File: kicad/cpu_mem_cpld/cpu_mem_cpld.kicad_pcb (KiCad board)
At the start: 2 copper layers, 160 x 100.3 mm, 33 parts, among them CON1 BARREL_JACK, J1 USB, P5 CONN_02X25, SW1 SW_PUSH, U1 65C02, U2 XC95108PC84, U3 28C256, U4 AS6C4008-55PCN, U5 74HC245, U6 LM555N, U7 74HCT00, X1 OSC

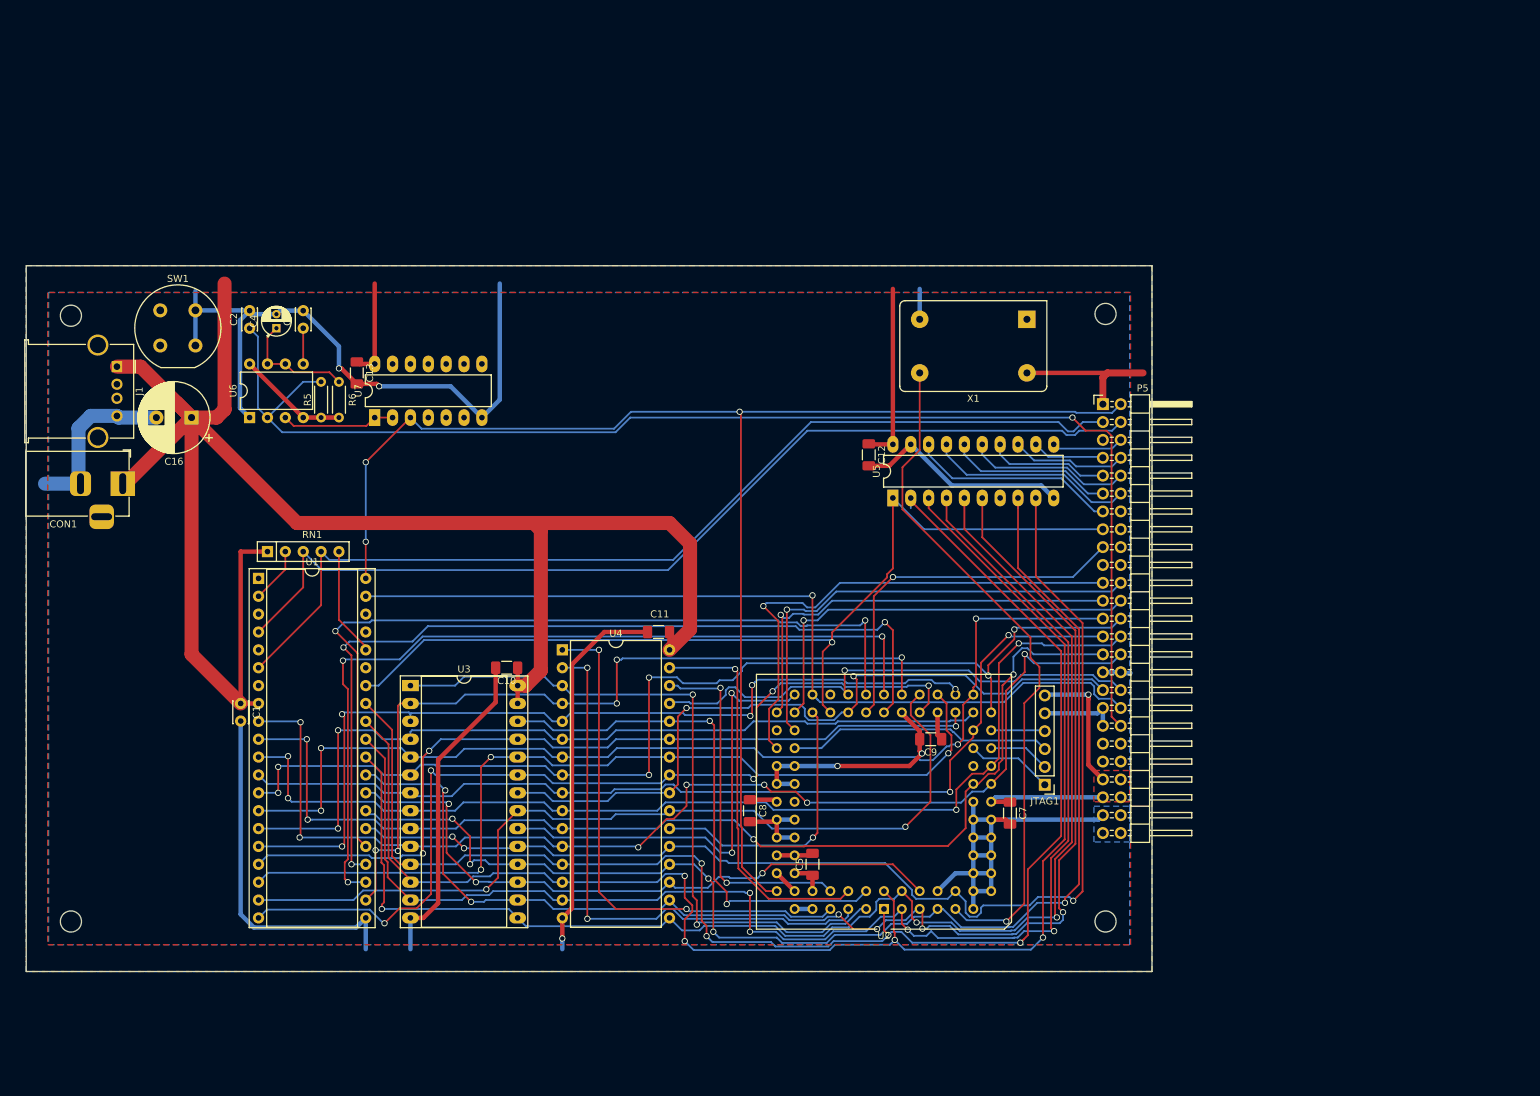
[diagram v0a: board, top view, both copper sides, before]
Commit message: cpld version with uart
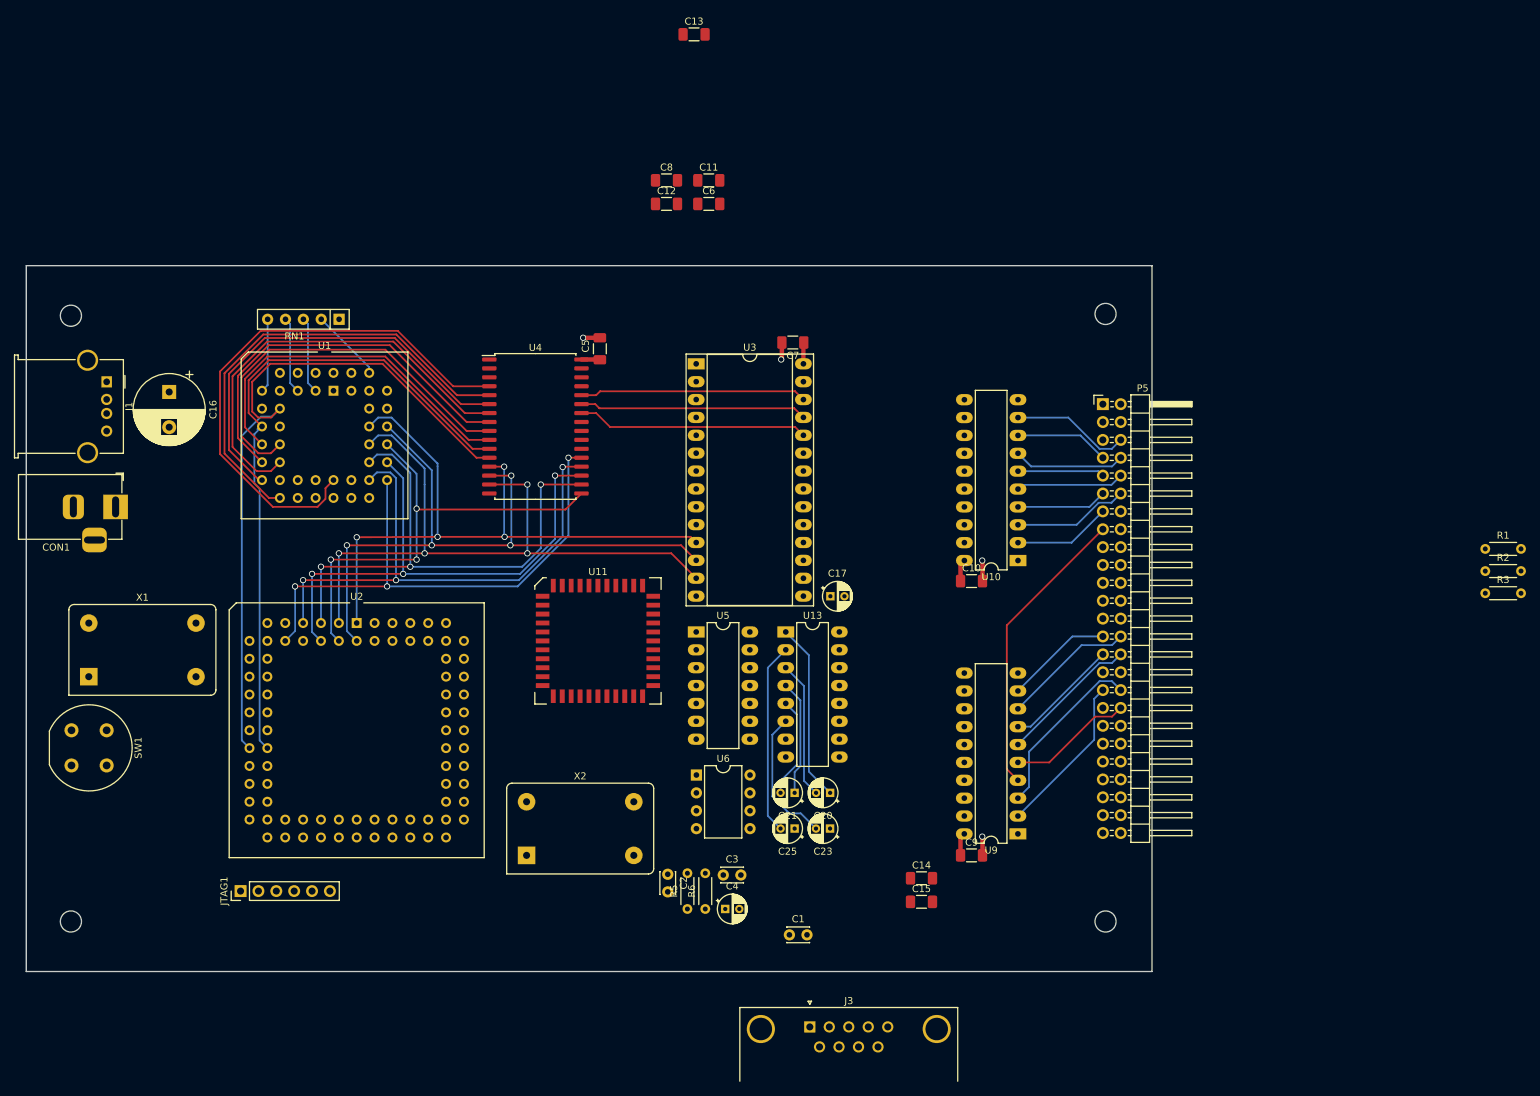
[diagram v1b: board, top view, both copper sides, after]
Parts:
- removed U7: 74HCT00, Package_DIP:DIP-14_W7.62mm_LongPads
- added C14: 100nF, Capacitor_SMD:C_1206_3216Metric_Pad1.33x1.80mm_HandSolder, F.Cu at (189.5, 132.8)
- added C15: 100nF, Capacitor_SMD:C_1206_3216Metric_Pad1.33x1.80mm_HandSolder, F.Cu at (189.5, 136.1)
- added C17: 1µF, Capacitor_THT:CP_Radial_D4.0mm_P2.00mm, F.Cu at (176.5, 92.7)
- added C20: 1µF, Capacitor_THT:CP_Radial_D4.0mm_P2.00mm, F.Cu at (176.5, 120.7)
- added C21: 1µF, Capacitor_THT:CP_Radial_D4.0mm_P2.00mm, F.Cu at (171.4, 120.7)
- added C23: 1µF, Capacitor_THT:CP_Radial_D4.0mm_P2.00mm, F.Cu at (176.5, 125.7)
- added C25: 1µF, Capacitor_THT:CP_Radial_D4.0mm_P2.00mm, F.Cu at (171.4, 125.7)
- added C6: 100n, Capacitor_SMD:C_1206_3216Metric_Pad1.33x1.80mm_HandSolder, F.Cu at (159.2, 36.9)
- added J3: DB9, Connector_Dsub:DSUB-9_Male_Horizontal_P2.77x2.84mm_EdgePinOffset4.94mm_Housed_MountingHolesOffset7.48mm, F.Cu at (173.6, 153.9)
- added R1: 4k7, Resistor_THT:R_Axial_DIN0204_L3.6mm_D1.6mm_P5.08mm_Horizontal, F.Cu at (269.6, 86.0)
- added R2: 4k7, Resistor_THT:R_Axial_DIN0204_L3.6mm_D1.6mm_P5.08mm_Horizontal, F.Cu at (269.6, 89.1)
- added R3: 3k3, Resistor_THT:R_Axial_DIN0204_L3.6mm_D1.6mm_P5.08mm_Horizontal, F.Cu at (269.6, 92.3)
- added U10: 74HC245, Package_DIP:DIP-20_W7.62mm_LongPads, F.Cu at (203.2, 87.6)
- added U11: 16550, Package_LCC:PLCC-44, F.Cu at (143.5, 99.1)
- added U13: MAX232, Package_DIP:DIP-16_W7.62mm_LongPads, F.Cu at (170.2, 97.8)
- added U9: 74HC245, Package_DIP:DIP-20_W7.62mm_LongPads, F.Cu at (203.2, 126.5)
- added X2: OSC, Oscillator:Oscillator_DIP-14_LargePads, F.Cu at (133.3, 129.5)
- U1: value 65C02 -> W65C02SxPL; footprint Package_DIP:DIP-40_W15.24mm_Socket -> Package_LCC:PLCC-44_THT-Socket
- U4: value AS6C4008-55PCN -> IS61C5128AS-25QLI; footprint Package_DIP:DIP-32_W15.24mm -> Package_SO:SSOP-32_11.305x20.495mm_P1.27mm
- U5: value 74HC245 -> 74LS06; footprint Package_DIP:DIP-20_W7.62mm_LongPads -> Package_DIP:DIP-14_W7.62mm_LongPads
- moved X1 142.7 mm to (71.1, 104.1), turned to 0 degrees
- moved JTAG1 115.3 mm to (92.7, 134.6), turned to 90 degrees
- moved C4 104.3 mm to (161.6, 137.2), turned to 0 degrees
- moved C3 98.0 mm to (161.3, 132.3), turned to 0 degrees
- moved C2 97.8 mm to (153.4, 132.2), turned to -90 degrees
- moved R6 91.2 mm to (158.8, 137.2), turned to 90 degrees
- moved C8 90.4 mm to (153.2, 33.6), turned to 0 degrees
- moved R5 87.1 mm to (156.2, 137.2)
- moved U2 85.3 mm to (109.2, 96.5), turned to 0 degrees
- moved C1 84.6 mm to (170.7, 140.8), turned to 0 degrees
- moved U6 81.3 mm to (157.5, 118.1), turned to 0 degrees
- moved C5 79.3 mm to (143.8, 57.5)
- moved C7 73.7 mm to (171.2, 56.6), turned to 180 degrees
- moved C13 67.9 mm to (157.2, 12.8), turned to 0 degrees
- moved C10 67.2 mm to (196.6, 90.6), turned to 0 degrees
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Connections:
- net /~CS_RAM renamed /~{CS_RAM}
- net /~CS_ROM renamed /~{CS_ROM}
- net ~CS_OPL renamed ~{CS_OPL}
- net ~CS_UART renamed ~{CS_UART}
- net ~CS_VDP renamed ~{CS_VDP}
- net ~CS_VIA renamed ~{CS_VIA}
- J1 pad 2: Net-(J1-Pad2) -> unconnected-(J1-Pad2)
- J1 pad 3: Net-(J1-Pad3) -> unconnected-(J1-Pad3)
- J1 pad 5: Net-(J1-Pad5) -> unconnected-(J1-Pad5)
- P5 pad 14: Net-(P5-Pad14) -> unconnected-(P5-Pad14)
- P5 pad 15: ~RW -> /Connector/R~{W}
- P5 pad 16: Net-(P5-Pad16) -> unconnected-(P5-Pad16)
- P5 pad 18: Net-(P5-Pad18) -> unconnected-(P5-Pad18)
- P5 pad 19: Net-(P5-Pad19) -> unconnected-(P5-Pad19)
- P5 pad 2: ~RESET -> ~{RESET}
- P5 pad 20: Net-(P5-Pad20) -> unconnected-(P5-Pad20)
- P5 pad 25: /CPU_A5 -> GND
- P5 pad 26: /CPU_A4 -> GND
- P5 pad 27: /CPU_A3 -> /Connector/A3
- P5 pad 28: /CPU_A2 -> /Connector/A2
- P5 pad 29: /CPU_A1 -> /Connector/A1
- P5 pad 3: ~NMI -> ~{NMI}
- P5 pad 30: /CPU_A0 -> /Connector/A0
- P5 pad 33: ~OE -> /Connector/~{OE}
- P5 pad 34: ~WE -> /Connector/~{WE}
- P5 pad 36: PHI2 -> /Connector/PHI2
- P5 pad 39: Net-(P5-Pad39) -> unconnected-(P5-Pad39)
- P5 pad 4: ~IRQ -> ~{IRQ}
- P5 pad 40: Net-(P5-Pad40) -> unconnected-(P5-Pad40)
- P5 pad 41: Net-(P5-Pad41) -> unconnected-(P5-Pad41)
- P5 pad 42: Net-(P5-Pad42) -> unconnected-(P5-Pad42)
- P5 pad 5: Net-(P5-Pad5) -> unconnected-(P5-Pad5)
- RN1 pad 2: RDY -> /~{BE}
- RN1 pad 3: ~IRQ -> RDY
- RN1 pad 4: ~NMI -> ~{IRQ}
- RN1 pad 5: /~BE -> ~{NMI}
- U1 pad 1: Net-(U1-Pad1) -> GND
- U1 pad 10: /CPU_A1 -> /CPU_A0
- U1 pad 11: /CPU_A2 -> /CPU_A1
- U1 pad 12: /CPU_A3 -> unconnected-(U1-Pad12)
- U1 pad 13: /CPU_A4 -> /CPU_A2
- U1 pad 14: /CPU_A5 -> /CPU_A3
- U1 pad 15: /CPU_A6 -> /CPU_A4
- U1 pad 16: /CPU_A7 -> /CPU_A5
- U1 pad 17: /CPU_A8 -> /CPU_A6
- U1 pad 18: /CPU_A9 -> /CPU_A7
- U1 pad 19: /CPU_A10 -> /CPU_A8
- U1 pad 2: RDY -> unconnected-(U1-Pad2)
- U1 pad 20: /CPU_A11 -> /CPU_A9
- U1 pad 21: GND -> /CPU_A10
- U1 pad 22: /CPU_A12 -> /CPU_A11
- U1 pad 23: /CPU_A13 -> GND
- U1 pad 24: /CPU_A14 -> GND
- U1 pad 25: /CPU_A15 -> /CPU_A12
- U1 pad 26: /D7 -> /CPU_A13
- U1 pad 27: /D6 -> /CPU_A14
- U1 pad 28: /D5 -> /CPU_A15
- U1 pad 29: /D4 -> /D7
- U1 pad 3: Net-(U1-Pad3) -> RDY
- U1 pad 30: /D3 -> /D6
- U1 pad 31: /D2 -> /D5
- U1 pad 32: /D1 -> /D4
- U1 pad 33: /D0 -> /D3
- U1 pad 34: ~RW -> /D2
- U1 pad 35: Net-(U1-Pad35) -> /D1
- U1 pad 36: /~BE -> /D0
- U1 pad 37: Net-(U1-Pad37) -> VCC
- U1 pad 38: Net-(U1-Pad38) -> ~{RW}
- U1 pad 39: PHI2 -> unconnected-(U1-Pad39)
- U1 pad 4: ~IRQ -> unconnected-(U1-Pad4)
- U1 pad 40: ~RESET -> /~{BE}
- U1 pad 5: Net-(U1-Pad5) -> ~{IRQ}
- U1 pad 6: ~NMI -> unconnected-(U1-Pad6)
- U1 pad 7: Net-(U1-Pad7) -> ~{NMI}
- U1 pad 8: VCC -> unconnected-(U1-Pad8)
- U1 pad 9: /CPU_A0 -> VCC
- U2 pad 47: ~WE -> ~{WE}
- U2 pad 48: ~OE -> ~{OE}
- U2 pad 50: ~RW -> ~{RW}
- U2 pad 56: /~CSW_VDP -> unconnected-(U2-Pad56)
- U2 pad 74: ~RESET -> ~{RESET}
- U3 pad 22: ~OE -> ~{OE}
- U4 pad 1: /EXT_A18 -> /EXT_A17
- U4 pad 24: ~OE -> ~{OE}
- U4 pad 29: ~WE -> ~{WE}
- U4 pad 30: /EXT_A17 -> /EXT_A18
- U5 pad 1: ~RW -> Net-(U11-Pad33)
- U5 pad 10: GND -> (no net)
- U5 pad 11: /Connector/D7 -> (no net)
- U5 pad 12: /Connector/D6 -> (no net)
- U5 pad 13: /Connector/D5 -> (no net)
- U5 pad 14: /Connector/D4 -> (no net)
- U5 pad 2: /D0 -> ~{IRQ}
- U5 pad 3: /D1 -> ~{RESET}
- U5 pad 4: /D2 -> Net-(R1-Pad2)
- U5 pad 5: /D3 -> Net-(U5-Pad5)
- U5 pad 6: /D4 -> ~{RESET}
- U5 pad 7: /D5 -> (no net)
- U5 pad 8: /D6 -> (no net)
- U5 pad 9: /D7 -> (no net)
- U6 pad 3: Net-(U6-Pad3) -> Net-(U5-Pad5)
- X1 pad 1: Net-(X1-Pad1) -> unconnected-(X1-Pad1)
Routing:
- net GND: track 439.1 -> 10.4 mm, vias 5 -> 4
- net VCC: track 380.8 -> 12.1 mm, vias 1 -> 0
- net ~RESET: track 200.0 -> 0.00 mm, vias 3 -> 0
- net /RESET_TRIG: track 188.0 -> 0.00 mm, vias 1 -> 0
- net ~NMI: track 141.0 -> 0.00 mm
- net ~IRQ: track 140.6 -> 0.00 mm
- net ~RW: track 135.9 -> 0.00 mm, vias 1 -> 0
- net /CPU_A11: track 133.3 -> 0.00 mm, vias 5 -> 0
- net /D3: track 196.7 -> 66.9 mm
- net /CPU_A14: track 126.0 -> 0.00 mm, vias 3 -> 0
- net /CPU_A10: track 125.2 -> 0.00 mm, vias 2 -> 0
- net PHI2: track 125.2 -> 0.00 mm, vias 1 -> 0
- net /CPU_A13: track 121.1 -> 0.00 mm, vias 3 -> 0
- net /CPU_A15: track 119.6 -> 0.00 mm, vias 2 -> 0
- net /D4: track 189.5 -> 75.9 mm, vias 6 -> 3
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- added copper zone on In1.Cu, net GND
- added copper zone on In2.Cu, net VCC
- removed copper zone on B.Cu, net GND
- removed copper zone on F.Cu, net VCC
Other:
- copper layers 2 -> 4
- net class Default removed
- net class vcc removed

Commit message: cpu cpld 512
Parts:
- removed CON1: BARREL_JACK, Connector_BarrelJack:BarrelJack_Horizontal
- removed J3: DB9, Connector_Dsub:DSUB-9_Male_Horizontal_P2.77x2.84mm_EdgePinOffset4.94mm_Housed_MountingHolesOffset7.48mm
- removed JTAG1: Conn_01x06_Male, Connector_PinHeader_2.54mm:PinHeader_1x06_P2.54mm_Vertical
- removed SW1: SW_PUSH, Button_Switch_THT:Push_E-Switch_KS01Q01
- added 5V: BARREL_JACK, Connector_BarrelJack:BarrelJack_Horizontal, F.Cu at (75.8, 94.3)
- added G***: LOGO, QRCODE:qrcode2, F.Cu at (102.9, 54.6)
- added JTAG: Conn_01x06_Male, Connector_PinHeader_2.54mm:PinHeader_1x06_P2.54mm_Vertical, F.Cu at (203.2, 142.2)
- added REF**: KiCad-Logo_5mm_SilkScreen, Symbol:KiCad-Logo_5mm_SilkScreen, F.Cu at (90.2, 141.0)
- added REF**: Polarity_Center_Positive_6mm_SilkScreen, Symbol:Polarity_Center_Positive_6mm_SilkScreen, F.Cu at (82.5, 69.8)
- added RESET: SW_PUSH, Button_Switch_THT:Push_E-Switch_KS01Q01, F.Cu at (71.1, 62.2)
- added SERIAL: DB9, Connector_Dsub:DSUB-9_Male_Horizontal_P2.77x2.84mm_EdgePinOffset4.94mm_Housed_MountingHolesOffset7.48mm, F.Cu at (71.5, 113.5)
- C1: footprint Capacitor_THT:C_Disc_D3.0mm_W2.0mm_P2.50mm -> Capacitor_SMD:C_1206_3216Metric_Pad1.33x1.80mm_HandSolder; moved to B.Cu
- C11, C13, C14, C6, C7, C9: moved to B.Cu
- RN1: value R_Network04 -> 3k3
- U1: value W65C02SxPL -> W65C02S
- U10, U9: value 74HC245 -> 74HCT245
- U11: footprint Package_LCC:PLCC-44 -> Package_LCC:PLCC-44_THT-Socket
- U2: value XC95108PC84 -> CHUCK
- U4: value IS61C5128AS-25QLI -> 512k x 8; footprint Package_SO:SSOP-32_11.305x20.495mm_P1.27mm -> Package_DIP:DIP-32_W15.24mm_LongPads
- U6: value LM555N -> NE555
- moved R3 196.0 mm to (77.5, 130.8)
- moved R1 159.3 mm to (110.5, 94.0), turned to 180 degrees
- moved R2 159.3 mm to (110.5, 96.5), turned to 180 degrees
- moved C9 103.0 mm to (111.8, 71.1), turned to -90 degrees
- moved C8 98.6 mm to (200.7, 120.0)
- moved C6 97.7 mm to (100.3, 114.9), turned to 90 degrees
- moved C20 96.9 mm to (80.0, 111.8), turned to -90 degrees
- moved C23 96.5 mm to (80.0, 124.5), turned to -90 degrees
- moved C4 95.7 mm to (99.1, 64.8), turned to 180 degrees
- moved C13 94.5 mm to (167.9, 106.7), turned to 180 degrees
- moved C25 93.7 mm to (80.0, 105.4), turned to -90 degrees
- moved C21 91.5 mm to (80.0, 118.1), turned to -90 degrees
- moved R5 90.9 mm to (87.6, 77.5)
- moved C2 89.0 mm to (94.0, 66.0), turned to 180 degrees
- moved C11 86.6 mm to (143.5, 118.7), turned to -90 degrees
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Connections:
- net ~{IRQ} renamed /~{IRQ}
- net ~{NMI} renamed /~{NMI}
- net ~{RESET} renamed /~{RESET}
- P5 pad 17: RDY -> /CPU_RDY
- P5 pad 21: ~{CS_OPL} -> /~{CS_OPL}
- P5 pad 22: ~{CS_VIA} -> /~{CS_VIA}
- P5 pad 23: ~{CS_UART} -> /~{CS_UART2}
- P5 pad 24: ~{CS_VDP} -> /~{CSR_VDP}
- RN1 pad 3: RDY -> /CPU_RDY
- U1 pad 3: RDY -> /CPU_RDY
- U1 pad 38: ~{RW} -> /CPU_R~{W}
- U1 pad 41: PHI2 -> /PHI2
- U10 pad 1: ~{RW} -> /CPU_RW
- U11 pad 16: ~{CS_UART} -> /~{CS_UART}
- U11 pad 20: ~{WE} -> /~{WE}
- U11 pad 24: ~{OE} -> /~{OE}
- U2 pad 10: /D7 -> unconnected-(U2-Pad10)
- U2 pad 11: GND -> unconnected-(U2-Pad11)
- U2 pad 12: GND -> unconnected-(U2-Pad12)
- U2 pad 13: GND -> /CPU_A14
- U2 pad 14: GND -> /CPU_RDY
- U2 pad 15: GND -> /CPU_A1
- U2 pad 17: GND -> /CPU_A8
- U2 pad 18: GND -> /EXT_A15
- U2 pad 19: GND -> /PHI2
- U2 pad 20: GND -> unconnected-(U2-Pad20)
- U2 pad 21: GND -> unconnected-(U2-Pad21)
- U2 pad 23: GND -> /D6
- U2 pad 24: /CPU_A0 -> unconnected-(U2-Pad24)
- U2 pad 25: /CPU_A1 -> /~{CS_RAM}
- U2 pad 26: /CPU_A2 -> /~{CS_UART}
- U2 pad 3: /D2 -> /CPU_A15
- U2 pad 31: /CPU_A3 -> /~{CS_ROM}
- U2 pad 32: /CPU_A4 -> unconnected-(U2-Pad32)
- U2 pad 33: /CPU_A5 -> /~{CS_VDP}
- U2 pad 34: /CPU_A6 -> unconnected-(U2-Pad34)
- U2 pad 35: /CPU_A7 -> /~{CS_OPL}
- U2 pad 36: /CPU_A8 -> unconnected-(U2-Pad36)
- U2 pad 37: /CPU_A9 -> /~{OE}
- U2 pad 39: /CPU_A10 -> /~{WE}
- U2 pad 4: /D3 -> unconnected-(U2-Pad4)
- U2 pad 40: /CPU_A11 -> unconnected-(U2-Pad40)
- U2 pad 41: /CPU_A12 -> unconnected-(U2-Pad41)
- U2 pad 43: /CPU_A13 -> /~{CS_VIA}
- U2 pad 44: /CPU_A14 -> /CPU_A9
- U2 pad 45: /CPU_A15 -> unconnected-(U2-Pad45)
- U2 pad 46: RDY -> /D2
- U2 pad 47: ~{WE} -> /EXT_A16
- U2 pad 48: ~{OE} -> /CPU_A4
- U2 pad 5: /D4 -> /EXT_A14
- U2 pad 50: ~{RW} -> unconnected-(U2-Pad50)
- U2 pad 51: PHI2 -> unconnected-(U2-Pad51)
- U2 pad 52: /~{CS_RAM} -> /EXT_A17
- U2 pad 53: /~{CS_ROM} -> /CPU_A6
- U2 pad 54: ~{CS_UART} -> unconnected-(U2-Pad54)
- U2 pad 55: ~{CS_VDP} -> unconnected-(U2-Pad55)
- U2 pad 56: unconnected-(U2-Pad56) -> /CPU_A12
- U2 pad 57: ~{CS_VIA} -> unconnected-(U2-Pad57)
- U2 pad 58: ~{CS_OPL} -> unconnected-(U2-Pad58)
- U2 pad 6: /D5 -> unconnected-(U2-Pad6)
- U2 pad 61: GND -> /EXT_A18
- U2 pad 62: GND -> unconnected-(U2-Pad62)
- U2 pad 63: GND -> unconnected-(U2-Pad63)
- U2 pad 65: GND -> /CPU_A10
- U2 pad 66: GND -> /CPU_A11
- U2 pad 67: GND -> unconnected-(U2-Pad67)
- U2 pad 68: GND -> /D4
- U2 pad 69: GND -> unconnected-(U2-Pad69)
- U2 pad 7: /D6 -> unconnected-(U2-Pad7)
- U2 pad 70: GND -> /CPU_A5
- U2 pad 71: GND -> /CPU_R~{W}
- U2 pad 72: GND -> /D3
- U2 pad 75: GND -> unconnected-(U2-Pad75)
- U2 pad 76: GND -> unconnected-(U2-Pad76)
- U2 pad 77: GND -> unconnected-(U2-Pad77)
- U2 pad 79: /EXT_A18 -> /D7
- U2 pad 80: /EXT_A17 -> unconnected-(U2-Pad80)
- U2 pad 81: /EXT_A16 -> /CPU_A0
- U2 pad 82: /EXT_A15 -> /D5
- U2 pad 83: /EXT_A14 -> /CPU_A7
- U2 pad 84: /EXT_A13 -> /CPU_A13
- U3 pad 22: ~{OE} -> /~{OE}
- U3 pad 26: /EXT_A13 -> /CPU_A13
- U4 pad 1: /EXT_A17 -> /EXT_A18
- U4 pad 24: ~{OE} -> /~{OE}
- U4 pad 28: /EXT_A13 -> /CPU_A13
- U4 pad 29: ~{WE} -> /~{WE}
- U4 pad 30: /EXT_A18 -> /EXT_A17
- U5 pad 10: (no net) -> unconnected-(U5-Pad10)
- U5 pad 11: (no net) -> GND
- U5 pad 12: (no net) -> unconnected-(U5-Pad12)
- U5 pad 13: (no net) -> GND
- U5 pad 14: (no net) -> VCC
- U5 pad 7: (no net) -> GND
- U5 pad 8: (no net) -> unconnected-(U5-Pad8)
- U5 pad 9: (no net) -> GND
- U9 pad 15: PHI2 -> /PHI2
- U9 pad 16: ~{RW} -> /CPU_R~{W}
- U9 pad 17: ~{WE} -> /~{WE}
- U9 pad 18: ~{OE} -> /~{OE}
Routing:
- net /~{WE}: track 0.00 -> 222.4 mm
- net /RESET_TRIG: track 0.00 -> 222.4 mm
- net /~{RESET}: track 0.00 -> 215.8 mm, vias 0 -> 1
- net /~{OE}: track 0.00 -> 185.2 mm, vias 0 -> 2
- net /D0: track 96.3 -> 258.7 mm, vias 4 -> 3
- net /CPU_A11: track 0.00 -> 154.6 mm, vias 0 -> 3
- net /CPU_A9: track 32.9 -> 183.4 mm, vias 0 -> 2
- net /~{IRQ}: track 10.9 -> 151.9 mm
- net /CPU_RDY: track 0.00 -> 139.7 mm, vias 0 -> 2
- net /~{CS_ROM}: track 0.00 -> 138.5 mm, vias 0 -> 2
- net /~{NMI}: track 10.5 -> 142.4 mm
- net /D3: track 66.9 -> 196.9 mm, vias 3 -> 4
- net /CPU_A10: track 0.00 -> 129.6 mm, vias 0 -> 5
- net /CPU_R~{W}: track 0.00 -> 126.9 mm, vias 0 -> 2
- net /EXT_A16: track 0.00 -> 114.1 mm, vias 0 -> 2
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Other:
- board text added: "GND"
- board text added: "Steckschwein 512k CPU/MEM/UART Board (C) 2022 Woinke / Lauke www.steckschwein.de"
- board text added: "TCK"
- board text added: "TDI"
- board text added: "TDO"
- board text added: "TMS"
- board text added: "VCC"
